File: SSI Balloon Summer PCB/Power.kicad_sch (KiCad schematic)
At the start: 35 parts, among them J1 Battery connector, Q2 DMG2305UX-7, SW1 SW_SPDT, U11 TPS63070RNMR, U12 TPS63070RNMR, U3 AP2112K-3.3TRG1

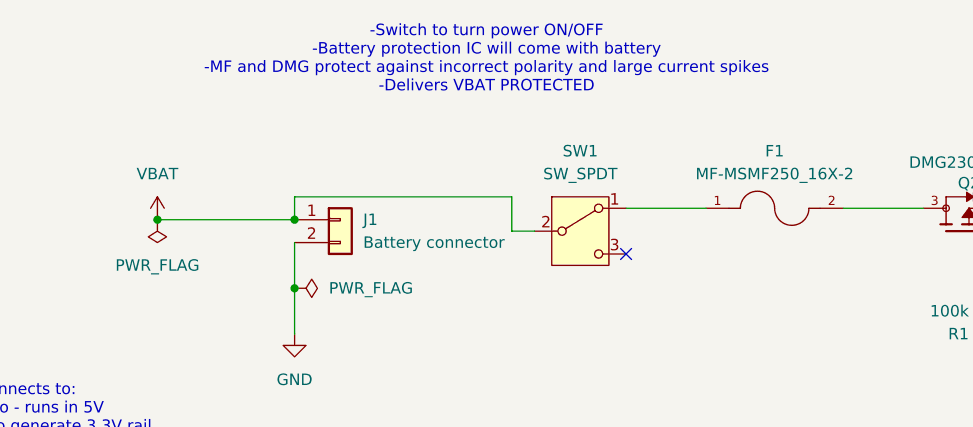
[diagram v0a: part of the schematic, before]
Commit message: Routing for power sheet
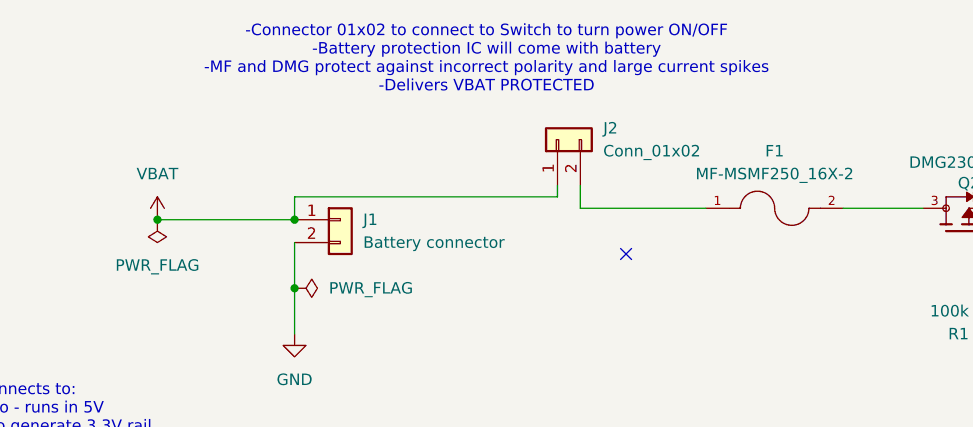
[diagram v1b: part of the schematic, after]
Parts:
- removed SW1: SW_SPDT, symbol Switch:SW_SPDT
- added J2: Conn_01x02, Connector_JST:JST_PH_B2B-PH-K_1x02_P2.00mm_Vertical, symbol Connector_Generic:Conn_01x02
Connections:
- net VBAT: now also J2.1 (Pin_1)
- net at F1.1: now also J2.2 (Pin_2)
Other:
- note added: "-Connector 01x02 to connect to Switch to turn power ON/OFF -Battery protection IC will come with battery -MF and DMG protect against incorrect polarity and large current spikes -Delivers VBAT PROTECTED"
- note removed: "-Switch to turn power ON/OFF -Battery protection IC will come with battery -MF and DMG protect against incorrect polarity and large current spikes -Delivers VBAT PROTECTED"
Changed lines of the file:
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@@
 	(generator_version "10.0")
 	(paper "A4")
-	(text "-Switch to turn power ON/OFF\n-Battery protection IC will come with battery\n-MF and DMG protect against incorrect polarity and large current spikes\n-Delivers VBAT PROTECTED\n"
+	(text "-Connector 01x02 to connect to Switch to turn power ON/OFF\n-Battery protection IC will come with battery\n-MF and DMG protect against incorrect polarity and large current spikes\n-Delivers VBAT PROTECTED\n"
 		(exclude_from_sim no)
 		(at 119.126 29.21 0)
@@
 	(wire
 		(pts
-			(xy 134.62 45.72) (xy 143.51 45.72)
-		)
-		(stroke
-			(width 0)
-			(type default)
-		)
-	)
-	(wire
-		(pts
 			(xy 64.77 104.14) (xy 62.23 104.14)
 		)
@@
 	(wire
 		(pts
-			(xy 121.92 44.45) (xy 121.92 48.26)
+			(xy 173.99 119.38) (xy 173.99 127)
 		)
 		(stroke
@@
 	(wire
 		(pts
-			(xy 173.99 119.38) (xy 173.99 127)
+			(xy 189.23 45.72) (xy 205.74 45.72)
 		)
 		(stroke
@@
 	(wire
 		(pts
-			(xy 189.23 45.72) (xy 205.74 45.72)
+			(xy 82.55 152.4) (xy 82.55 156.21)
 		)
 		(stroke
@@
 	(wire
 		(pts
-			(xy 82.55 152.4) (xy 82.55 156.21)
+			(xy 129.54 45.72) (xy 129.54 43.18)
 		)
 		(stroke
@@
 	(wire
 		(pts
-			(xy 170.18 116.84) (xy 170.18 119.38)
+			(xy 127 44.45) (xy 127 43.18)
 		)
 		(stroke
@@
 	(wire
 		(pts
-			(xy 121.92 48.26) (xy 124.46 48.26)
+			(xy 170.18 116.84) (xy 170.18 119.38)
 		)
 		(stroke
@@
 	(wire
 		(pts
-			(xy 97.79 44.45) (xy 121.92 44.45)
+			(xy 97.79 44.45) (xy 127 44.45)
 		)
 		(stroke
@@
 	(wire
 		(pts
+			(xy 129.54 45.72) (xy 143.51 45.72)
+		)
+		(stroke
+			(width 0)
+			(type default)
+		)
+	)
+	(wire
+		(pts
 			(xy 227.33 142.24) (xy 233.68 142.24)
 		)
@@
 	)
 	(symbol
-		(lib_id "Switch:SW_SPDT")
-		(at 129.54 48.26 0)
-		(unit 1)
-		(body_style 1)
-		(exclude_from_sim no)
-		(in_bom yes)
-		(on_board yes)
-		(in_pos_files yes)
-		(dnp no)
-		(fields_autoplaced yes)
-		(property "Reference" "SW1"
-			(at 129.54 39.37 0)
-			(show_name no)
-			(do_not_autoplace no)
-			(effects
-				(font
-					(size 1.27 1.27)
-				)
-			)
-		)
-		(property "Value" "SW_SPDT"
-			(at 129.54 41.91 0)
-			(show_name no)
-			(do_not_autoplace no)
-			(effects
-				(font
-					(size 1.27 1.27)
-				)
-			)
-		)
-		(property "Footprint" ""
-			(at 129.54 48.26 0)
-			(hide yes)
-			(show_name no)
-			(do_not_autoplace no)
-			(effects
-				(font
-					(size 1.27 1.27)
-				)
-			)
-		)
-		(property "Datasheet" ""
-			(at 129.54 55.88 0)
-			(hide yes)
-			(show_name no)
-			(do_not_autoplace no)
-			(effects
-				(font
-					(size 1.27 1.27)
-				)
-			)
-		)
-		(property "Description" "Switch, single pole double throw"
-			(at 129.54 48.26 0)
-			(hide yes)
-			(show_name no)
-			(do_not_autoplace no)
-			(effects
-				(font
-					(size 1.27 1.27)
-				)
-			)
-		)
-		(pin "1"
-		)
-		(pin "3"
-		)
-		(pin "2"
-		)
-		(instances
-			(project "SSI Summer Balloons"
-				(path "/3c45a535-6e6b-4825-ad52-82c10cbe7866/1b5737e2-4399-496a-b942-ad94430e2078"
-					(reference "SW1")
-					(unit 1)
-				)
-			)
-		)
-	)
-	(symbol
 		(lib_id "power:PWR_FLAG")
 		(at 205.74 45.72 180)
@@
 					(unit 1)
 				)
+			)
+		)
+	)
+	(symbol
+		(lib_id "Connector_Generic:Conn_01x02")
+		(at 127 38.1 90)
+		(unit 1)
+		(body_style 1)
+		(exclude_from_sim no)
+		(in_bom yes)
+		(on_board yes)
+		(in_pos_files yes)
+		(dnp no)
+		(fields_autoplaced yes)
+		(property "Reference" "J2"
+			(at 132.08 36.8299 90)
+			(show_name no)
+			(do_not_autoplace no)
+			(effects
+				(font
+					(size 1.27 1.27)
+				)
+				(justify right)
+			)
+		)
+		(property "Value" "Conn_01x02"
+			(at 132.08 39.3699 90)
+			(show_name no)
+			(do_not_autoplace no)
+			(effects
+				(font
+					(size 1.27 1.27)
+				)
+				(justify right)
+			)
+		)
+		(property "Footprint" "Connector_JST:JST_PH_B2B-PH-K_1x02_P2.00mm_Vertical"
+			(at 127 38.1 0)
+			(hide yes)
+			(show_name no)
+			(do_not_autoplace no)
+			(effects
+				(font
+					(size 1.27 1.27)
+				)
+			)
+		)
+		(property "Datasheet" ""
+			(at 127 38.1 0)
+			(hide yes)
+			(show_name no)
+			(do_not_autoplace no)
+			(effects
+				(font
+					(size 1.27 1.27)
+				)
+			)
+		)
+		(property "Description" "Generic connector, single row, 01x02, script generated (kicad-library-utils/schlib/autogen/connector/)"
+			(at 127 38.1 0)
+			(hide yes)
+			(show_name no)
+			(do_not_autoplace no)
+			(effects
+				(font
+					(size 1.27 1.27)
+				)
+			)
+		)
+		(pin "2"
+		)
+		(pin "1"
+		)
+		(instances
+			(project "SSI Summer Balloons"
+				(path "/3c45a535-6e6b-4825-ad52-82c10cbe7866/1b5737e2-4399-496a-b942-ad94430e2078"
+					(reference "J2")
+					(unit 1)
+				)

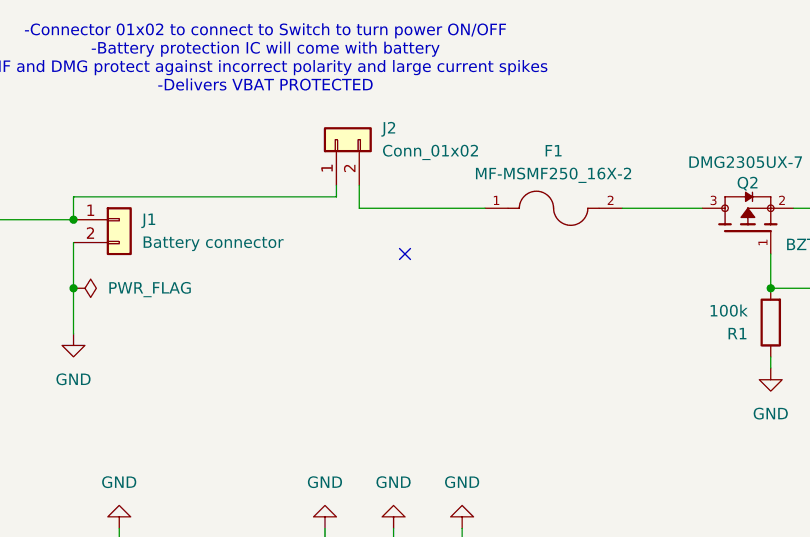
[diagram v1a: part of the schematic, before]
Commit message: Routed 4v1 and 3v3 rail
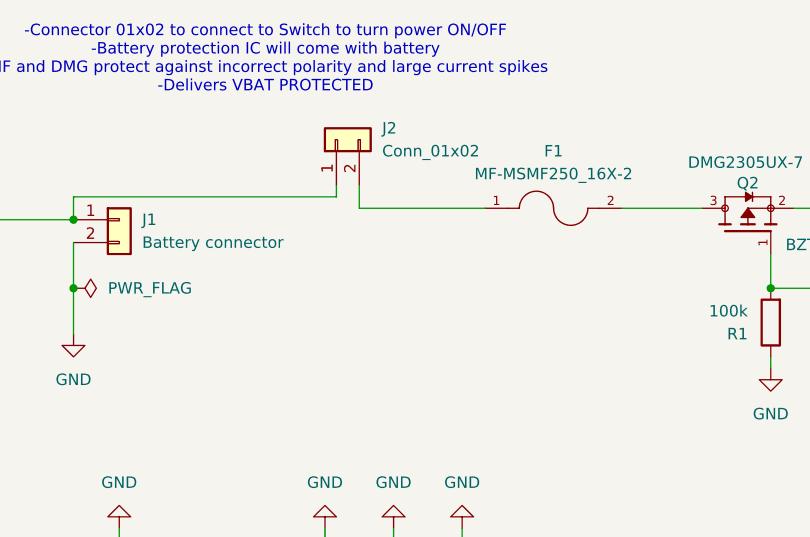
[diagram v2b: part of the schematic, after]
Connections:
- no-connect marks 5 -> 4
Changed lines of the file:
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@@
-	)
-	(no_connect
-		(at 134.62 50.8)
 	)
 	(no_connect
